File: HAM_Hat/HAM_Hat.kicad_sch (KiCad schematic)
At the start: 65 parts, among them J101 TL212V-02P-G12S, J102 DB-9RS-C, J104 SMA6252A2, J106 Conn_01x01, J107 Conn_01x01, J3 FHDH2.54-40, M101 Fan, Q101 BSS138, Q102 BSS138, Q103 BSS138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

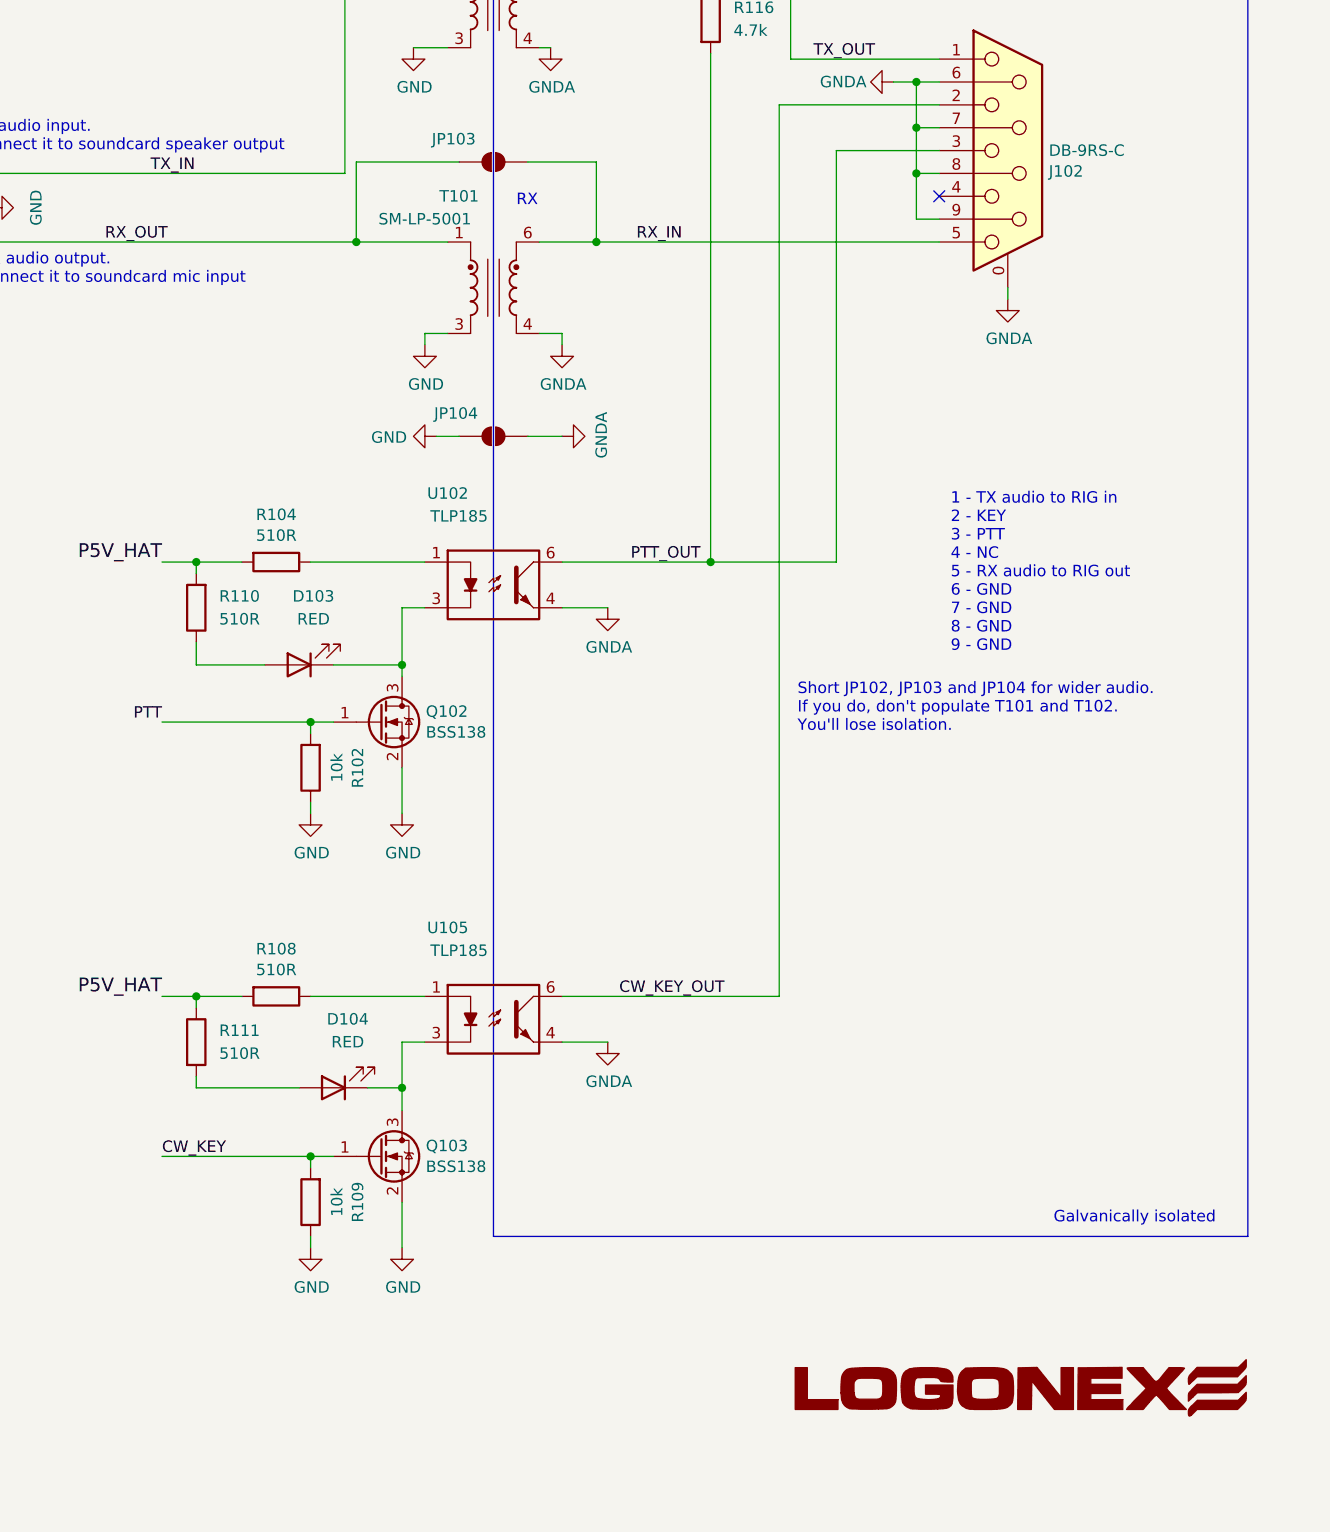
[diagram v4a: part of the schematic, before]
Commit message: Add DC decoupling capactiors
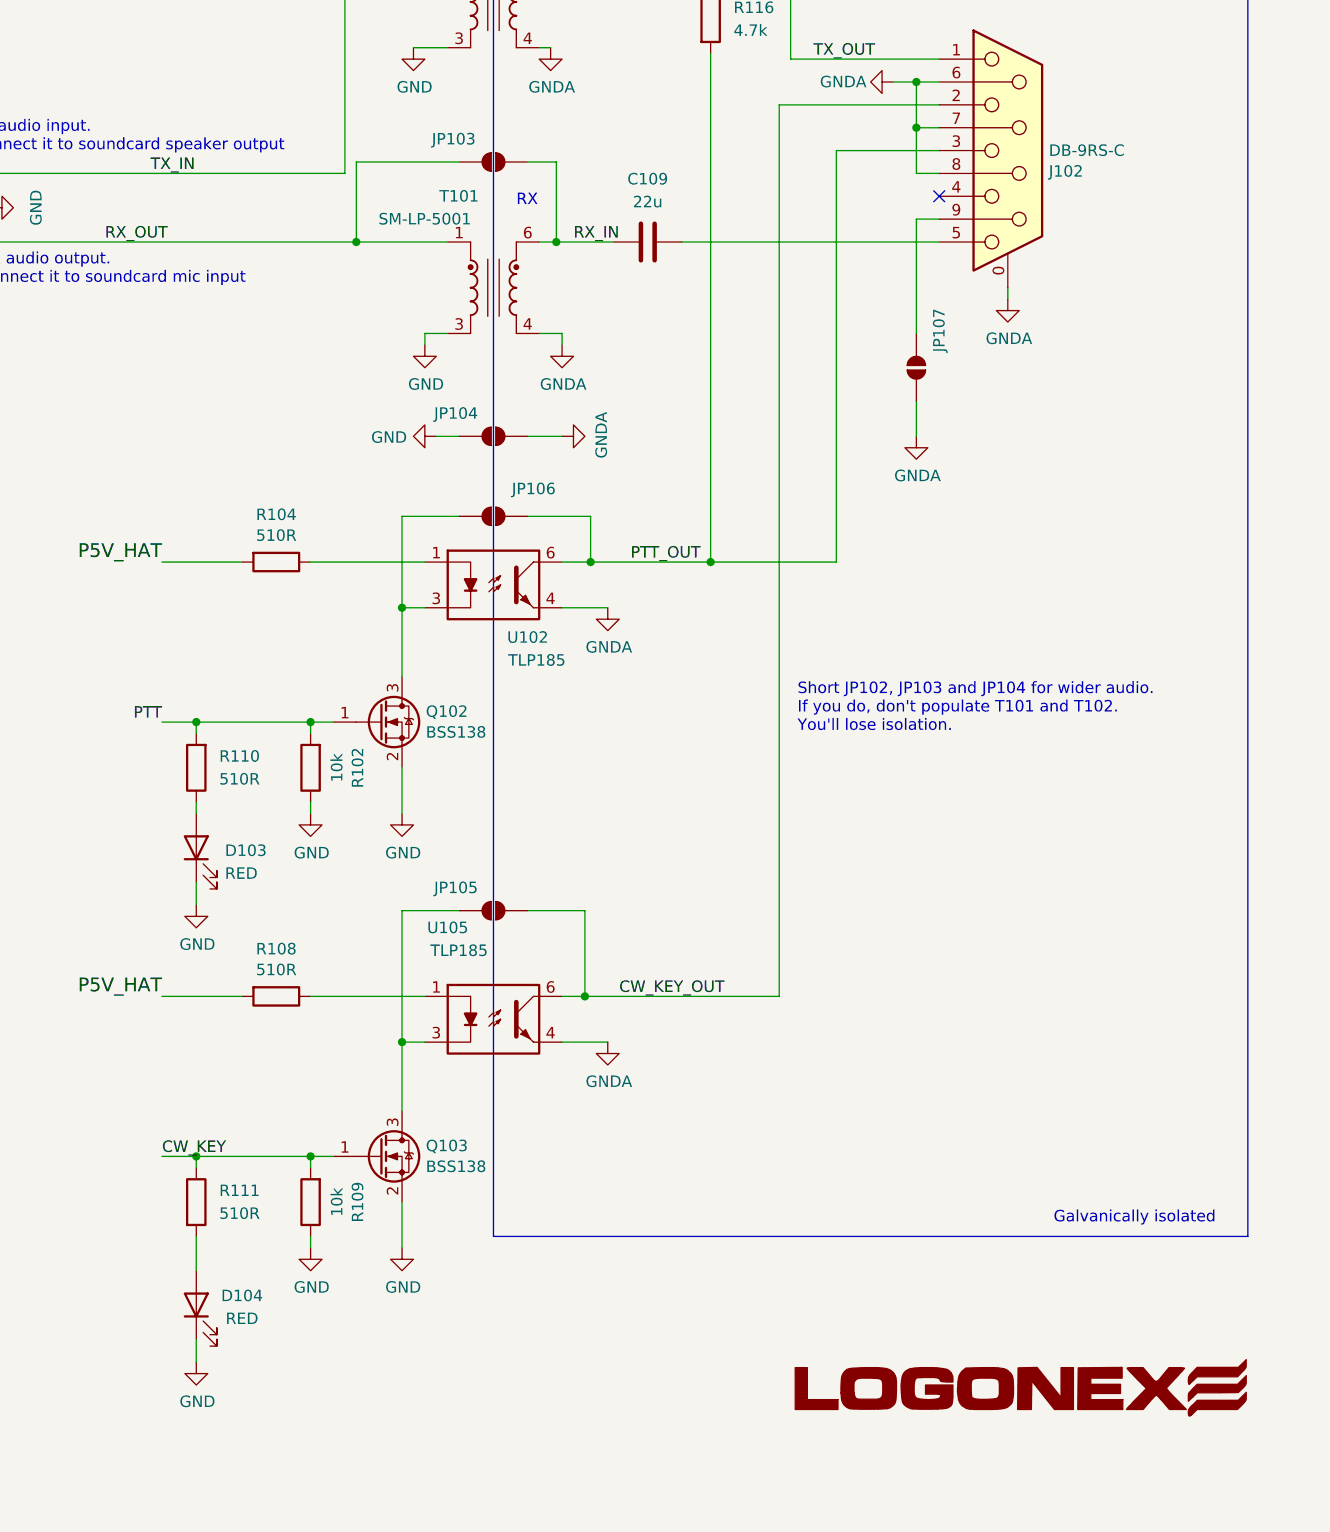
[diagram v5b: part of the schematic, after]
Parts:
- added C109: 22u, Capacitor_SMD:C_1206_3216Metric, symbol default:levcsi_database/340
- added JP105, JP106, JP107: SolderJumper_2_Open, Jumper:SolderJumper-2_P1.3mm_Open_RoundedPad1.0x1.5mm, symbol Jumper:SolderJumper_2_Open
- J105: value (none) -> ~
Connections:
- net CW_KEY: now also R111.1
- net CW_KEY_OUT: now also JP105.2 (B)
- net GND: now also D103.1 (K), D104.1 (K)
- net GNDA: now also JP107.2 (B); no longer J102.9
- net P5V_HAT: no longer R110.2, R111.1
- net PTT: now also R110.2
- net PTT_OUT: now also JP106.2 (B)
- net RX_IN: now also C109.2; no longer J102.5
- net at Q102.3 (D), U102.3: now also JP106.1 (A); no longer D103.1 (K)
- net at Q103.3 (D), U105.3: now also JP105.1 (A); no longer D104.1 (K)
- new net: C109.1, J102.5
- new net: J102.9, JP107.1 (A)
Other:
- note removed: "1 - TX audio to RIG in 2 - KEY 3 - PTT 4 - NC 5 - RX audio to RIG out 6 - GND 7 - GND 8 - GND 9 - GND"
- moved on the sheet: D103, D104, R110, R111
